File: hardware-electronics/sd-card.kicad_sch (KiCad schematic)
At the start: 40 parts, among them J5 Micro_SD_Card_Det_Hirose_DM3AT, U6 24AA04T-I_OT, U9 USB2244-AEZG-06, Y3 ECS-240-10-47-CKM-TR

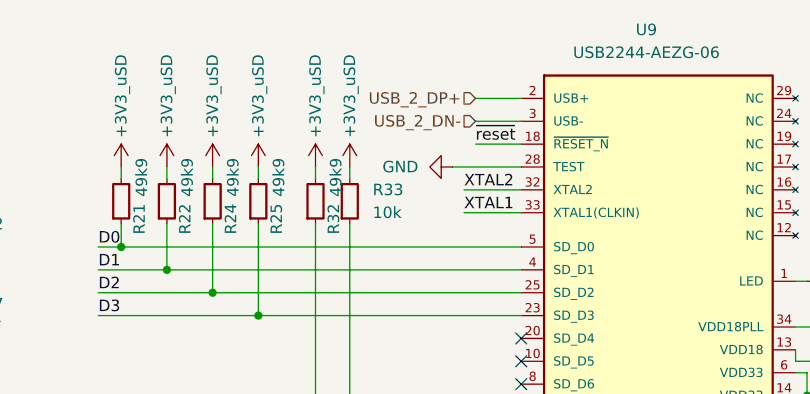
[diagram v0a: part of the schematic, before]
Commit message: [#17] SCH update USB net names
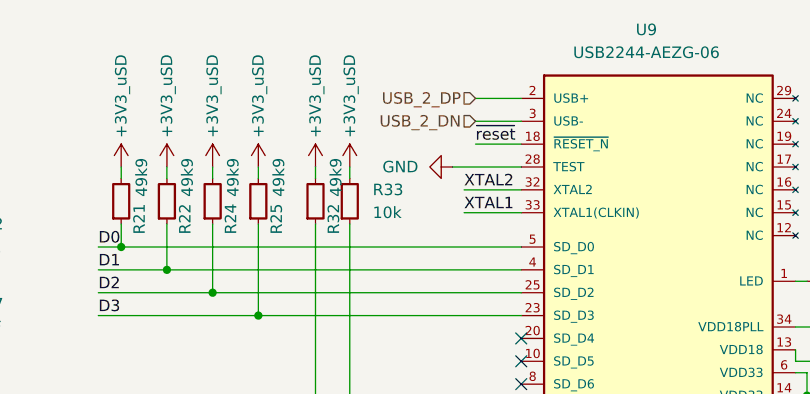
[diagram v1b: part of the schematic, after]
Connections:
- net USB_2_DN- renamed USB_2_DN
- net USB_2_DP+ renamed USB_2_DP
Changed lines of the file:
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@@
 		)
 	)
-	(hierarchical_label "USB_2_DP+"
+	(hierarchical_label "USB_2_DP"
 		(shape input)
 		(at 137.16 54.61 180)
@@
 		)
 	)
-	(hierarchical_label "USB_2_DN-"
+	(hierarchical_label "USB_2_DN"
 		(shape input)
 		(at 137.16 57.15 180)

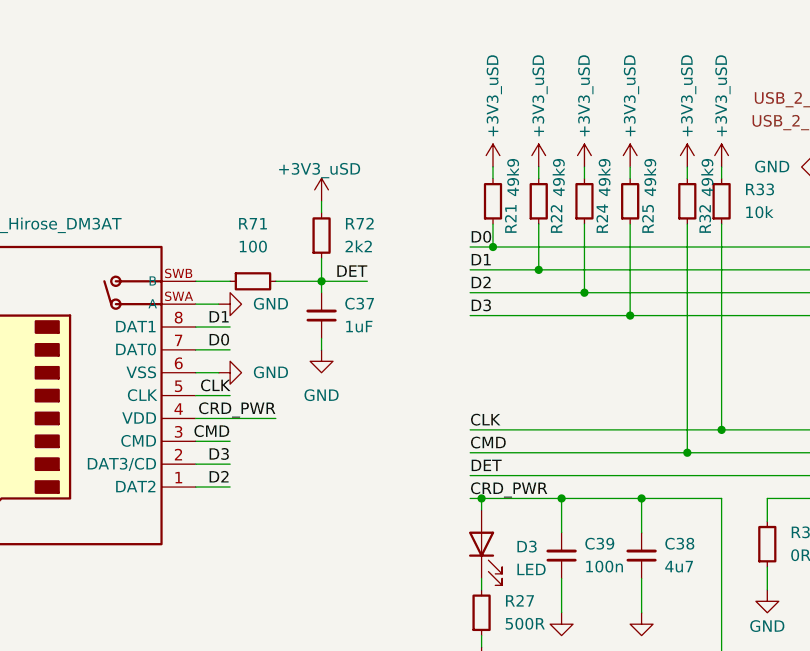
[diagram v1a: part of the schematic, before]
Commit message: [#17] Routing uSD data lines WIP
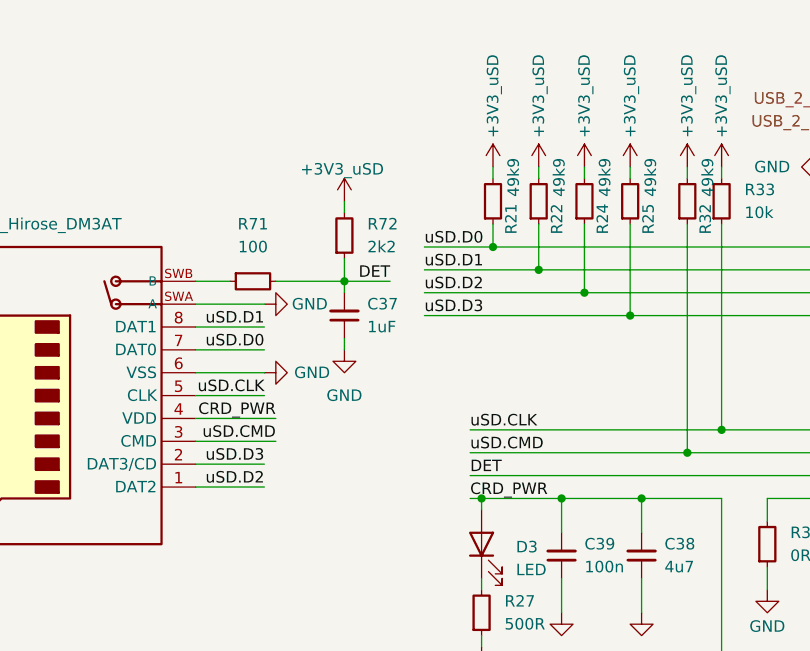
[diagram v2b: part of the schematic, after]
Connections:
- net CLK renamed uSD.CLK
- net CMD renamed uSD.CMD
- net D0 renamed uSD.D0
- net D1 renamed uSD.D1
- net D2 renamed uSD.D2
- net D3 renamed uSD.D3
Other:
- moved on the sheet: C37, R72

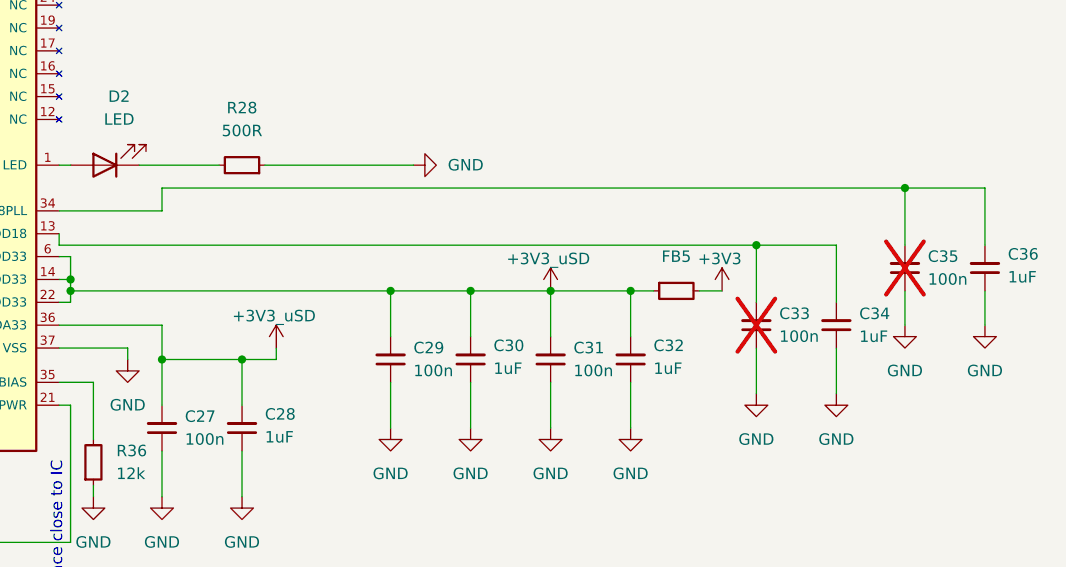
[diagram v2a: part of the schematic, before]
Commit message: [#17] eMMC lenght matching WIP
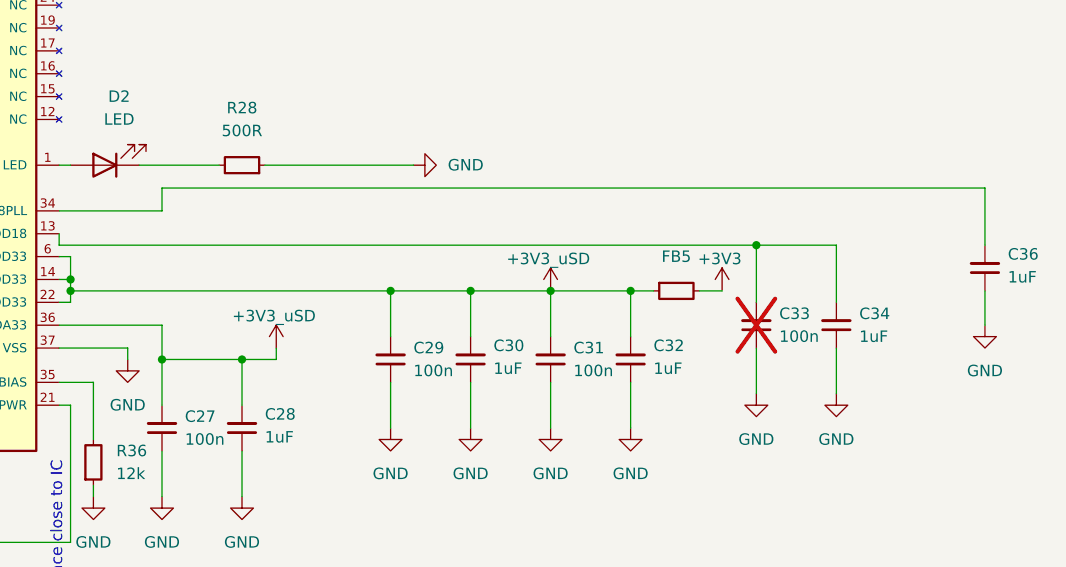
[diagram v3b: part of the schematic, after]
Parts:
- removed C35: C_100n_0402, M2SmartHomeFootprints:C_0402, symbol M2SmartHomeSymbols:C_100n_0402

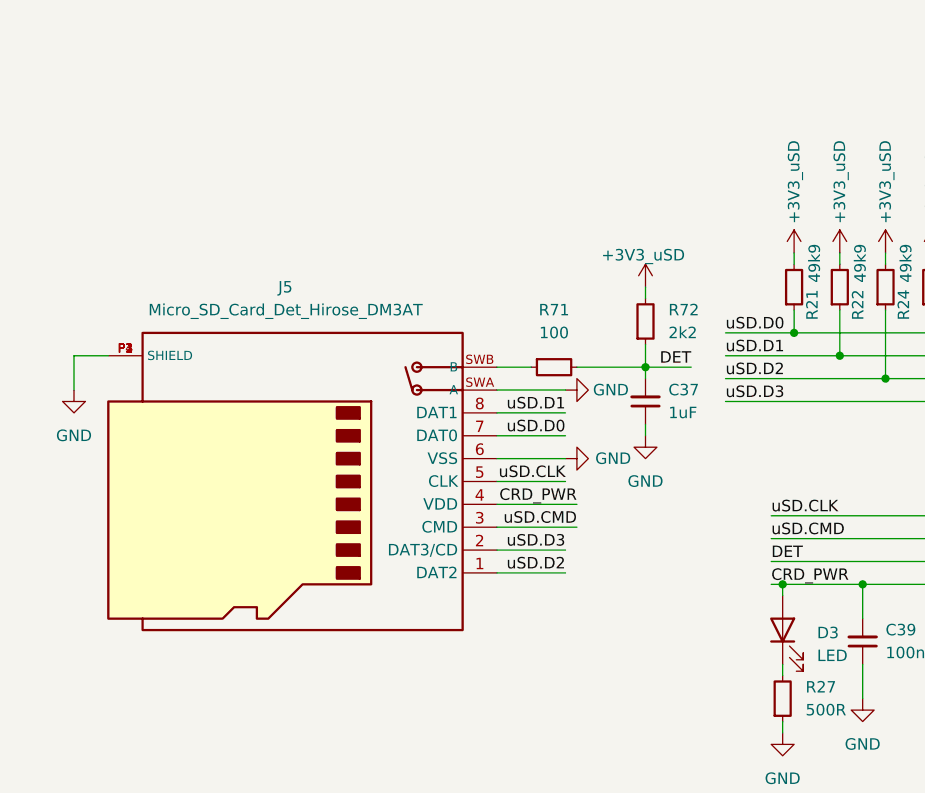
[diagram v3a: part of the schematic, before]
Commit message: [#20] PCB add pullup filtration cap on uSD datalines
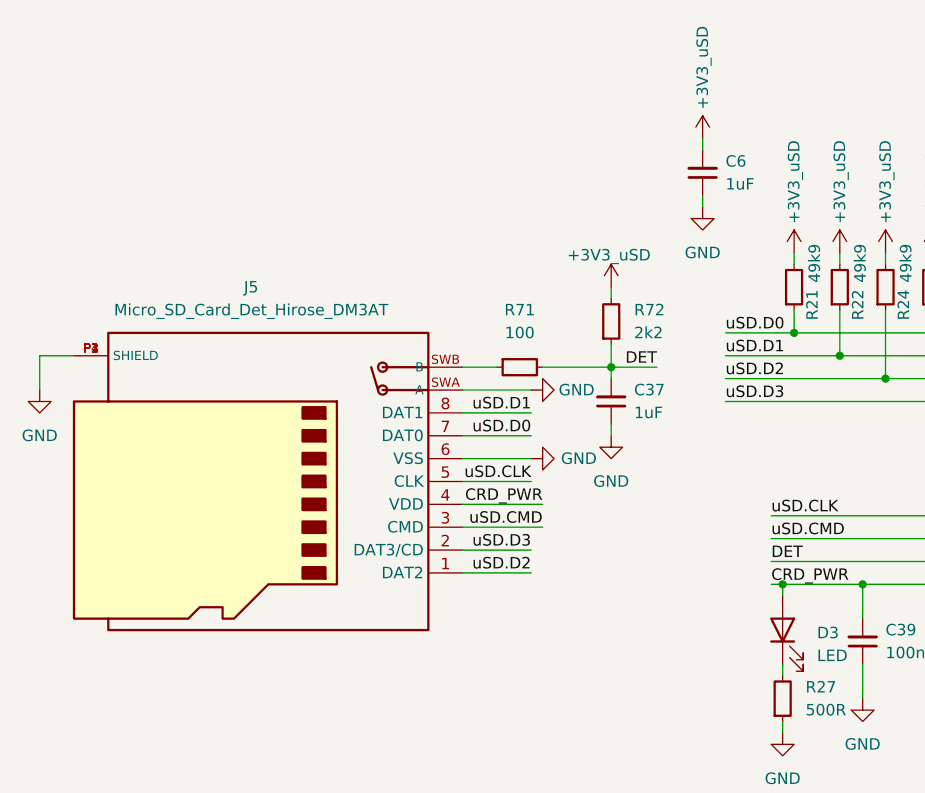
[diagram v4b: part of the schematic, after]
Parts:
- added C6: C_1uF_0402, M2SmartHomeFootprints:C_0402, symbol M2SmartHomeSymbols:C_1uF_0402
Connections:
- net +3V3_uSD: now also C6.2
- net GND: now also C6.1
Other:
- moved on the sheet: C37, J5, R71, R72

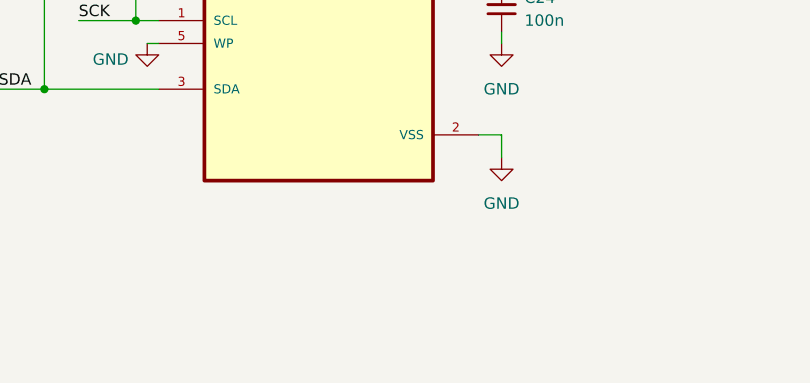
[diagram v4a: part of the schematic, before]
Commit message: [#24] PCB tag-connect programming connectors brainstorming
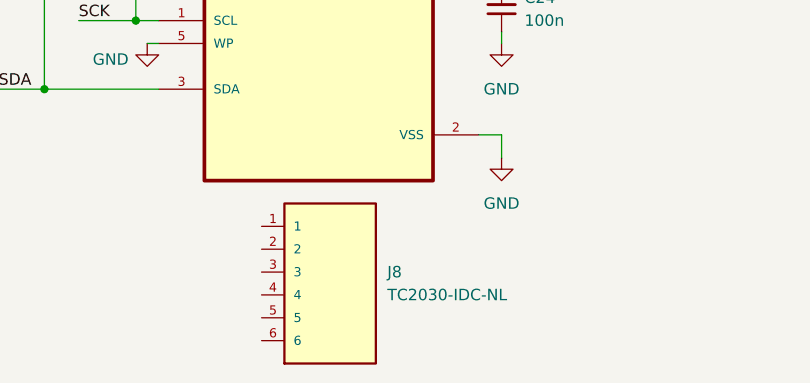
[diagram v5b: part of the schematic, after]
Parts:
- added J8: TC2030-IDC-NL, M2SmartHomeFootprints:TAG_TC2030-IDC-NL, symbol M2SmartHomeSymbols:TC2030-IDC-NL
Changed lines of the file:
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@@
+	)
+	(symbol
+		(lib_id "M2SmartHomeSymbols:TC2030-IDC-NL")
+		(at 143.51 191.77 0)
+		(unit 1)
+		(exclude_from_sim no)
+		(in_bom yes)
+		(on_board yes)
+		(dnp no)
+		(fields_autoplaced yes)
+		(property "Reference" "J8"
+			(at 149.86 189.2299 0)
+			(effects
+				(font
+					(size 1.27 1.27)
+				)
+				(justify left)
+			)
+		)
+		(property "Value" "TC2030-IDC-NL"
+			(at 149.86 191.7699 0)
+			(effects
+				(font
+					(size 1.27 1.27)
+				)
+				(justify left)
+			)
+		)
+		(property "Footprint" "M2SmartHomeFootprints:TAG_TC2030-IDC-NL"
+			(at 143.51 191.77 0)
+			(effects
+				(font
+					(size 1.27 1.27)
+				)
+				(justify bottom)
+				(hide yes)
+			)
+		)
+		(property "Datasheet" ""
+			(at 143.51 191.77 0)
+			(effects
+				(font
+					(size 1.27 1.27)
+				)
+				(hide yes)
+			)
+		)
+		(property "Description" ""
+			(at 143.51 191.77 0)
+			(effects
+				(font
+					(size 1.27 1.27)
+				)
+				(hide yes)
+			)
+		)
+		(property "MF" "Tag-Connect"
+			(at 143.51 191.77 0)
+			(effects
+				(font
+					(size 1.27 1.27)
+				)
+				(justify bottom)
+				(hide yes)
+			)
+		)
+		(property "Description_1" "\n                        \n                            PLUG-OF-NAILS 6-PIN W/O LEGS 8\n                        \n"
+			(at 143.51 191.77 0)
+			(effects
+				(font
+					(size 1.27 1.27)
+				)
+				(justify bottom)
+				(hide yes)
+			)
+		)
+		(property "Package" "None"
+			(at 143.51 191.77 0)
+			(effects
+				(font
+					(size 1.27 1.27)
+				)
+				(justify bottom)
+				(hide yes)
+			)
+		)
+		(property "Price" "None"
+			(at 143.51 191.77 0)
+			(effects
+				(font
+					(size 1.27 1.27)
+				)
+				(justify bottom)
+				(hide yes)
+			)
+		)
+		(property "Check_prices" "https://www.snapeda.com/parts/TC2030-IDC-NL/Tag-Connect/view-part/?ref=eda"
+			(at 143.51 191.77 0)
+			(effects
+				(font
+					(size 1.27 1.27)
+				)
+				(justify bottom)
+				(hide yes)
+			)
+		)
+		(property "STANDARD" "Manufacturer recommendation"
+			(at 143.51 191.77 0)
+			(effects
+				(font
+					(size 1.27 1.27)
+				)
+				(justify bottom)
+				(hide yes)
+			)
+		)
+		(property "PARTREV" "MS"
+			(at 143.51 191.77 0)
+			(effects
+				(font
+					(size 1.27 1.27)
+				)
+				(justify bottom)
+				(hide yes)
+			)
+		)
+		(property "SnapEDA_Link" "https://www.snapeda.com/parts/TC2030-IDC-NL/Tag-Connect/view-part/?ref=snap"
+			(at 143.51 191.77 0)
+			(effects
+				(font
+					(size 1.27 1.27)
+				)
+				(justify bottom)
+				(hide yes)
+			)
+		)
+		(property "MP" "TC2030-IDC-NL"
+			(at 143.51 191.77 0)
+			(effects
+				(font
+					(size 1.27 1.27)
+				)
+				(justify bottom)
+				(hide yes)
+			)
+		)
+		(property "Availability" "Not in stock"
+			(at 143.51 191.77 0)
+			(effects
+				(font
+					(size 1.27 1.27)
+				)
+				(justify bottom)
+				(hide yes)
+			)
+		)
+		(property "MANUFACTURER" "Tag-Connect"
+			(at 143.51 191.77 0)
+			(effects
+				(font
+					(size 1.27 1.27)
+				)
+				(justify bottom)
+				(hide yes)
+			)
+		)
+		(pin "6"
+		)
+		(pin "2"
+		)
+		(pin "5"
+		)
+		(pin "4"
+		)
+		(pin "3"
+		)
+		(pin "1"
+		)
+		(instances
+			(project "M2SmartHome"
+				(path "/da663dec-9e91-4003-a791-431d460ad63c/2a53ffe2-5715-44b3-b464-b3185e5be86d"
+					(reference "J8")
+					(unit 1)
+				)
+			)
+		)
 	)
 	(symbol

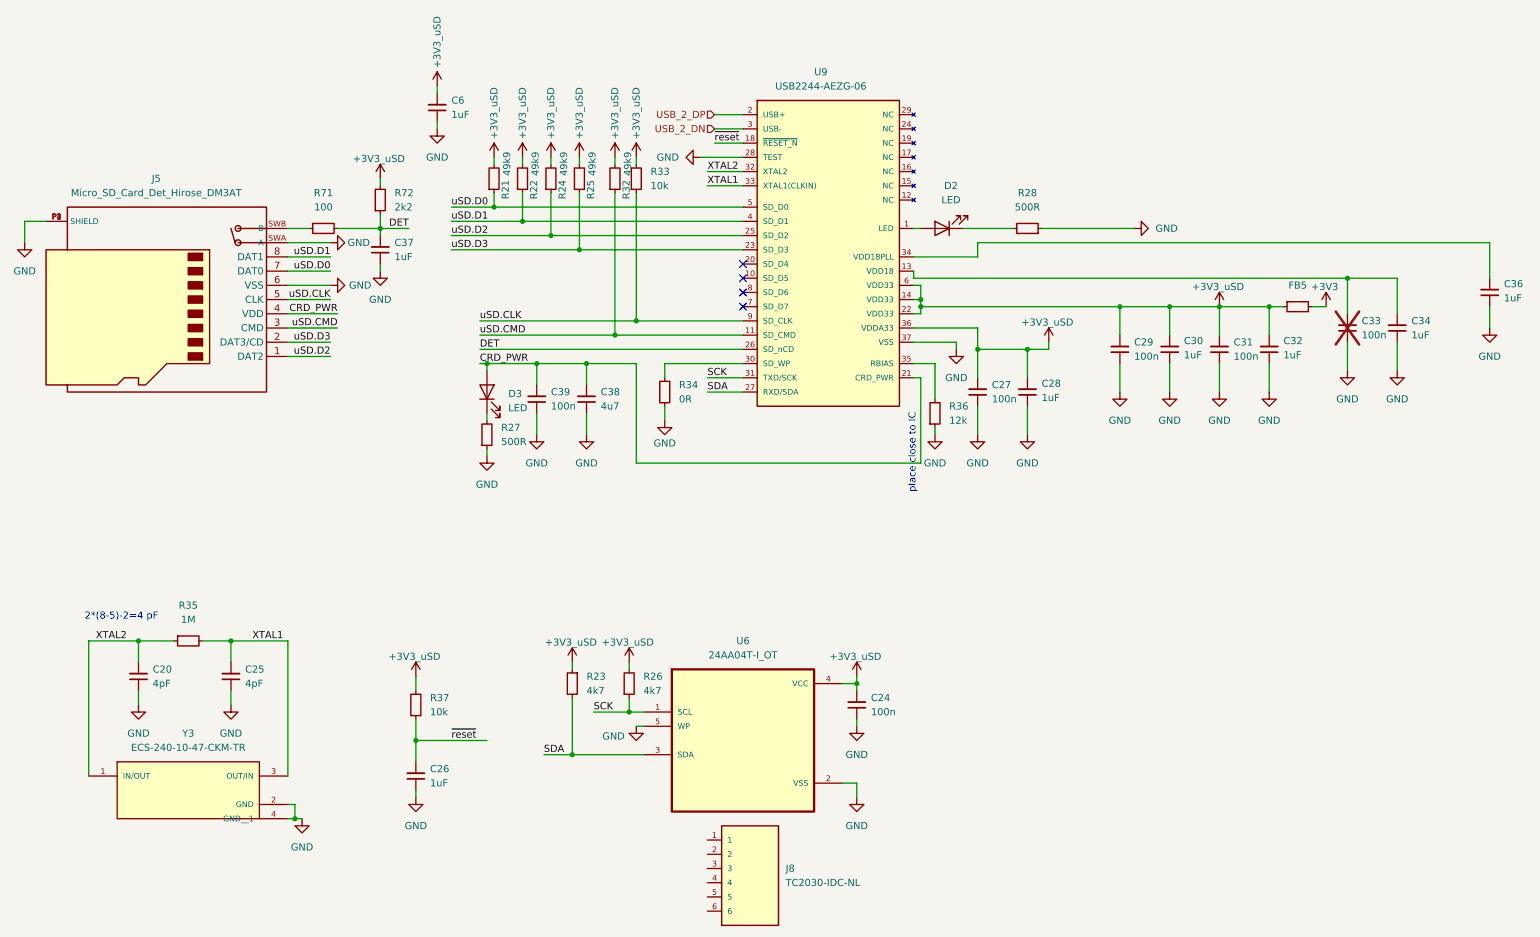
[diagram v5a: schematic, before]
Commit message: [#26] Remove power plane splits for invidual devices
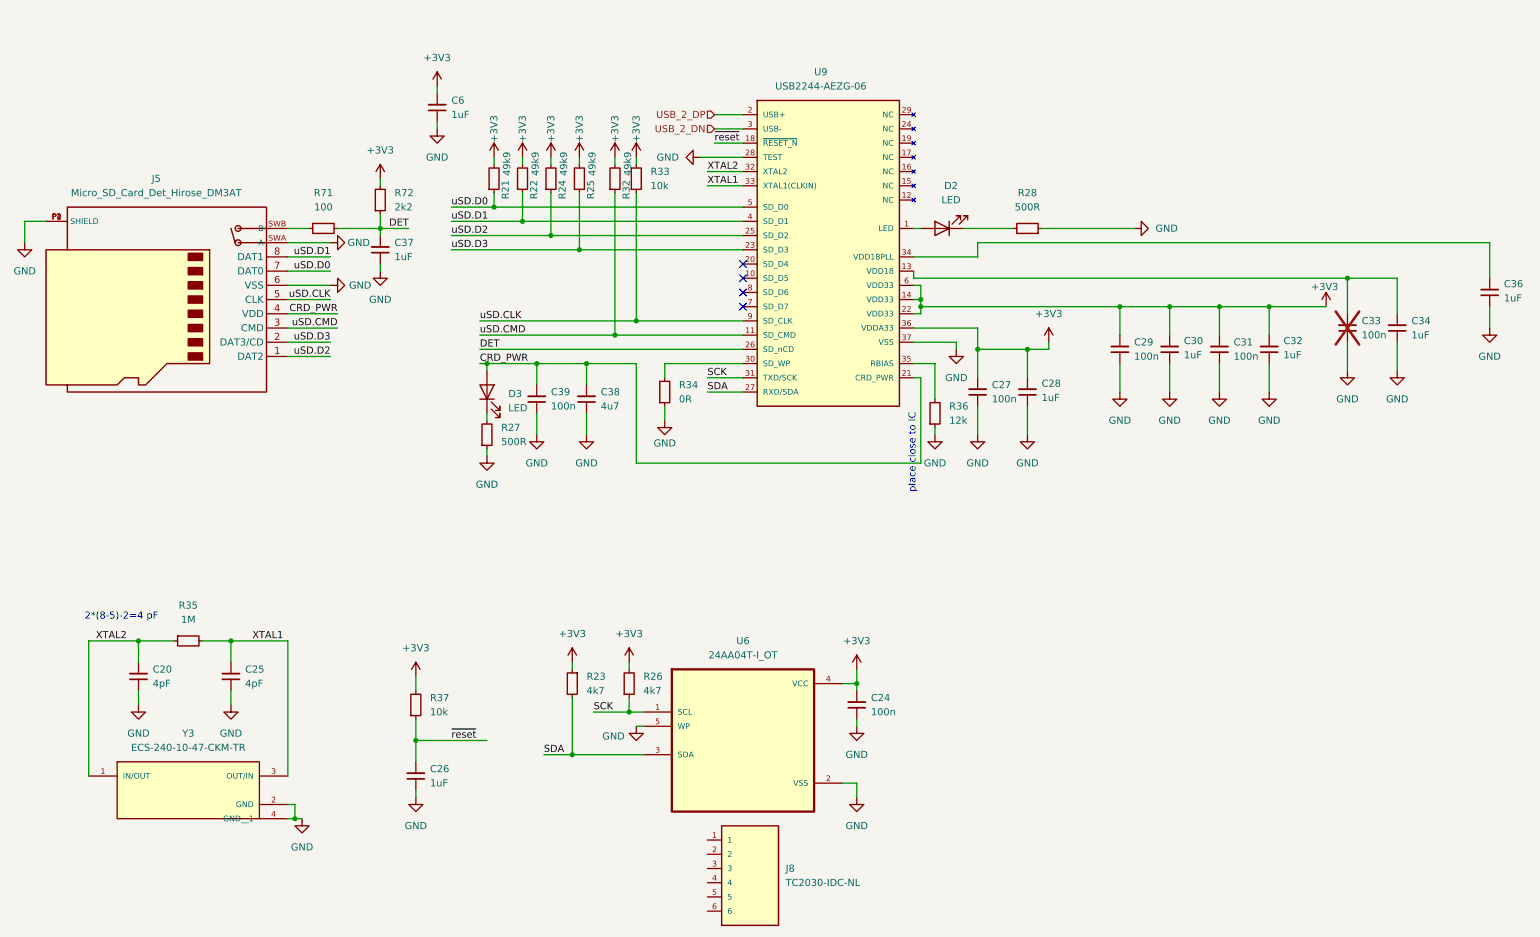
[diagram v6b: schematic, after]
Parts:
- removed FB5: FB_120R_0603, M2SmartHomeFootprints:FB_0603, symbol M2SmartHomeSymbols:FB_120R_0603
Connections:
- net +3V3_uSD is gone; now on net +3V3: C24.2, C27.2, C28.2, C29.2, C30.2, C31.2, C32.2, C6.2, R21.2, R22.2, R23.1, R24.2, R25.2, R26.2, R32.2, R33.2, R37.2, R72.2, U6.4 (VCC), U9.14 (VDD33), U9.22 (VDD33), U9.36 (VDDA33), U9.6 (VDD33)
